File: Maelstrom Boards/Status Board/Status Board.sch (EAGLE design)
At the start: 14 parts, among them P1 39-30-04

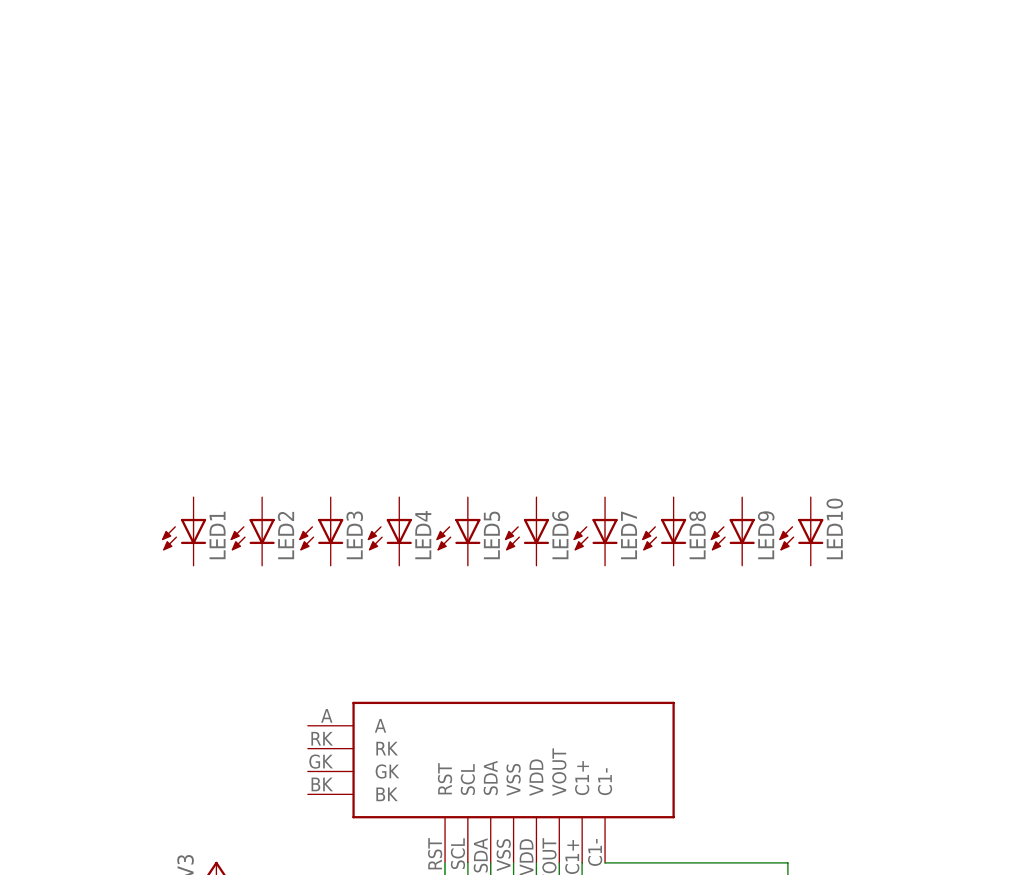
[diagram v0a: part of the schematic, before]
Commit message: Adding LEDs
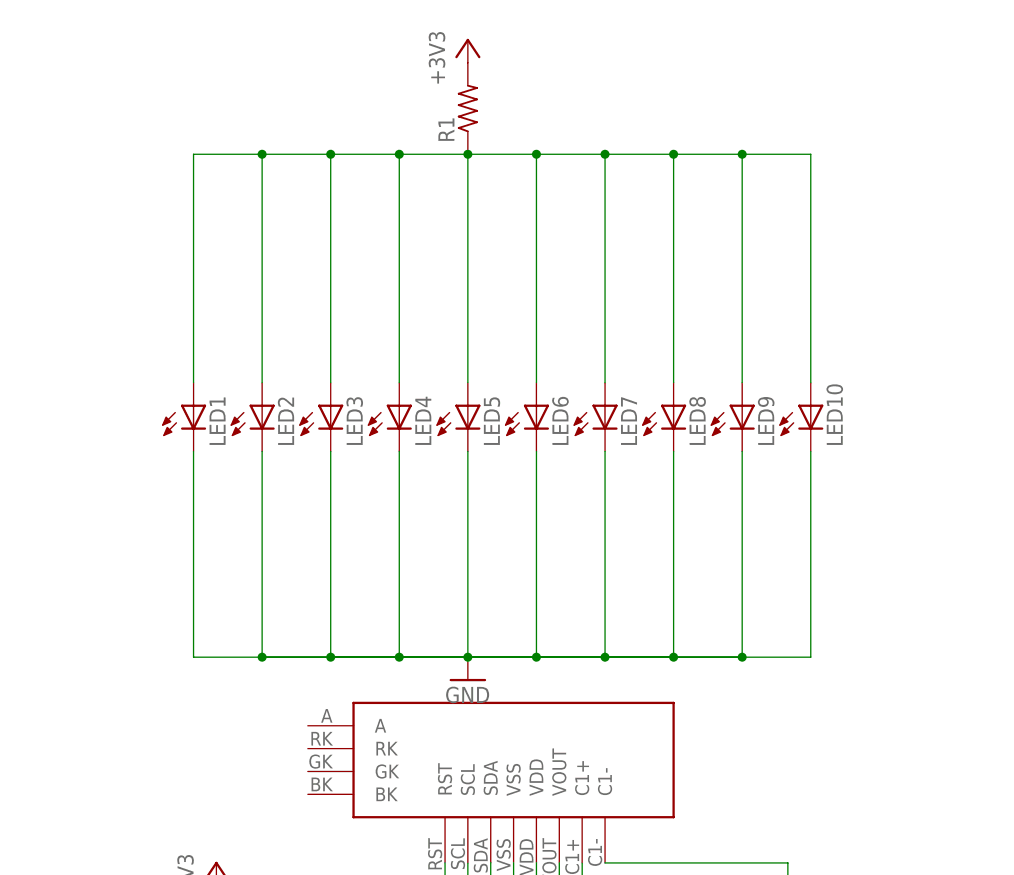
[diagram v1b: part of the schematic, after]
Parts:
- added R1: (no value), rcl:R-US_M3216
- LED1, LED10, LED2, LED3, LED4, LED5, LED6, LED7, LED8, LED9: device led:LEDCHIPLED-0603-TTW -> led:LEDCHIPLED_0603
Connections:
- new net N$4: LED1.A, LED10.A, LED2.A, LED3.A, LED4.A, LED5.A, LED6.A, LED7.A, LED8.A, LED9.A, R1.1
- net +3V3: now also R1.2
- net GND: now also LED1.C, LED10.C, LED2.C, LED3.C, LED4.C, LED5.C, LED6.C, LED7.C, LED8.C, LED9.C
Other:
- moved on the sheet: LED1, LED10, LED2, LED3, LED4, LED5, LED6, LED7, LED8, LED9

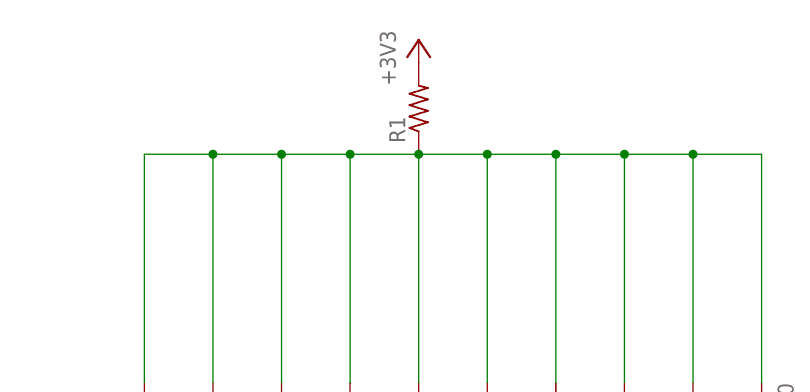
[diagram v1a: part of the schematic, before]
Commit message: Removing Resistor
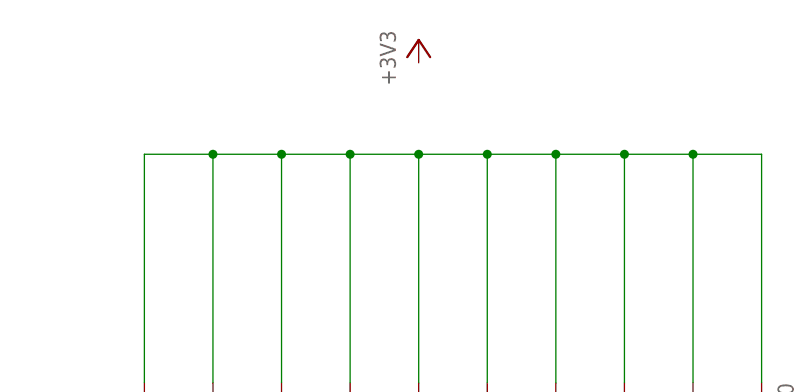
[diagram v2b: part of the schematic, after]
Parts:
- removed R1: (no value), rcl:R-US_M3216
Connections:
- net +3V3: no longer R1.2
- net N$4: no longer R1.1
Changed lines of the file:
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@@
 <part name="LED10" library="led" library_urn="urn:adsk.eagle:library:259" deviceset="LED" device="CHIPLED_0603" package3d_urn="urn:adsk.eagle:package:15822/2"/>
 <part name="GND3" library="supply1" library_urn="urn:adsk.eagle:library:371" deviceset="GND" device=""/>
-<part name="R1" library="rcl" library_urn="urn:adsk.eagle:library:334" deviceset="R-US_" device="M3216" package3d_urn="urn:adsk.eagle:package:23563/1"/>
 <part name="+3V3" library="supply1" library_urn="urn:adsk.eagle:library:371" deviceset="+3V3" device=""/>
 </parts>
@@
 <attribute name="VALUE" x="162.56" y="154.94" size="1.778" layer="96"/>
 </instance>
-<instance part="R1" gate="G$1" x="165.1" y="220.98" smashed="yes" rot="R90">
-<attribute name="NAME" x="163.6014" y="217.17" size="1.778" layer="95" rot="R90"/>
-<attribute name="VALUE" x="168.402" y="217.17" size="1.778" layer="96" rot="R90"/>
-</instance>
 <instance part="+3V3" gate="G$1" x="165.1" y="228.6" smashed="yes">
 <attribute name="VALUE" x="162.56" y="223.52" size="1.778" layer="96" rot="R90"/>
@@
 <wire x1="162.56" y1="137.16" x2="162.56" y2="134.62" width="0.1524" layer="91"/>
 <junction x="162.56" y="134.62"/>
-</segment>
-<segment>
-<pinref part="+3V3" gate="G$1" pin="+3V3"/>
-<pinref part="R1" gate="G$1" pin="2"/>
 </segment>
 </net>
@@
 <junction x="187.96" y="215.9"/>
 <junction x="195.58" y="215.9"/>
-<pinref part="R1" gate="G$1" pin="1"/>
 </segment>
 </net>

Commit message: Update Status Board
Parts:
- added R1: 23.333333, rcl:R-US_M3216
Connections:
- net +3V3: now also R1.2
- net N$4: now also R1.1
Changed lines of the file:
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@@
 <part name="LED10" library="led" library_urn="urn:adsk.eagle:library:259" deviceset="LED" device="CHIPLED_0603" package3d_urn="urn:adsk.eagle:package:15822/2"/>
 <part name="GND3" library="supply1" library_urn="urn:adsk.eagle:library:371" deviceset="GND" device=""/>
+<part name="R1" library="rcl" library_urn="urn:adsk.eagle:library:334" deviceset="R-US_" device="M3216" package3d_urn="urn:adsk.eagle:package:23563/1" value="23.333333"/>
 <part name="+3V3" library="supply1" library_urn="urn:adsk.eagle:library:371" deviceset="+3V3" device=""/>
 </parts>
@@
 <attribute name="VALUE" x="208.915" y="183.388" size="1.778" layer="96" rot="R90"/>
 </instance>
-<instance part="GND3" gate="1" x="165.1" y="157.48" smashed="yes">
-<attribute name="VALUE" x="162.56" y="154.94" size="1.778" layer="96"/>
+<instance part="GND3" gate="1" x="165.1" y="165.1" smashed="yes">
+<attribute name="VALUE" x="162.56" y="162.56" size="1.778" layer="96"/>
+</instance>
+<instance part="R1" gate="G$1" x="165.1" y="220.98" smashed="yes" rot="R90">
+<attribute name="NAME" x="163.6014" y="217.17" size="1.778" layer="95" rot="R90"/>
+<attribute name="VALUE" x="168.402" y="217.17" size="1.778" layer="96" rot="R90"/>
 </instance>
 <instance part="+3V3" gate="G$1" x="165.1" y="228.6" smashed="yes">
@@
 <junction x="162.56" y="134.62"/>
 </segment>
+<segment>
+<pinref part="+3V3" gate="G$1" pin="+3V3"/>
+<pinref part="R1" gate="G$1" pin="2"/>
+</segment>
 </net>
 <net name="GND" class="0">
@@
 <pinref part="LED5" gate="G$1" pin="C"/>
 <pinref part="GND3" gate="1" pin="GND"/>
-<wire x1="165.1" y1="182.88" x2="165.1" y2="160.02" width="0.1524" layer="91"/>
+<wire x1="165.1" y1="182.88" x2="165.1" y2="167.64" width="0.1524" layer="91"/>
 <pinref part="LED4" gate="G$1" pin="C"/>
-<wire x1="157.48" y1="182.88" x2="157.48" y2="160.02" width="0.1524" layer="91"/>
-<wire x1="157.48" y1="160.02" x2="165.1" y2="160.02" width="0.1524" layer="91"/>
-<junction x="165.1" y="160.02"/>
+<wire x1="157.48" y1="182.88" x2="157.48" y2="167.64" width="0.1524" layer="91"/>
+<junction x="165.1" y="167.64"/>
 <pinref part="LED3" gate="G$1" pin="C"/>
-<wire x1="149.86" y1="182.88" x2="149.86" y2="160.02" width="0.1524" layer="91"/>
-<wire x1="149.86" y1="160.02" x2="157.48" y2="160.02" width="0.1524" layer="91"/>
+<wire x1="149.86" y1="182.88" x2="149.86" y2="167.64" width="0.1524" layer="91"/>
 <pinref part="LED2" gate="G$1" pin="C"/>
-<wire x1="157.48" y1="160.02" x2="165.1" y2="160.02" width="0.1524" layer="91"/>
-<wire x1="142.24" y1="182.88" x2="142.24" y2="160.02" width="0.1524" layer="91"/>
-<wire x1="142.24" y1="160.02" x2="149.86" y2="160.02" width="0.1524" layer="91"/>
+<wire x1="142.24" y1="182.88" x2="142.24" y2="167.64" width="0.1524" layer="91"/>
 <pinref part="LED1" gate="G$1" pin="C"/>
-<wire x1="149.86" y1="160.02" x2="157.48" y2="160.02" width="0.1524" layer="91"/>
-<wire x1="157.48" y1="160.02" x2="165.1" y2="160.02" width="0.1524" layer="91"/>
-<wire x1="134.62" y1="182.88" x2="134.62" y2="160.02" width="0.1524" layer="91"/>
-<wire x1="134.62" y1="160.02" x2="142.24" y2="160.02" width="0.1524" layer="91"/>
+<wire x1="134.62" y1="182.88" x2="134.62" y2="167.64" width="0.1524" layer="91"/>
+<wire x1="134.62" y1="167.64" x2="142.24" y2="167.64" width="0.1524" layer="91"/>
 <pinref part="LED6" gate="G$1" pin="C"/>
-<wire x1="142.24" y1="160.02" x2="149.86" y2="160.02" width="0.1524" layer="91"/>
-<wire x1="149.86" y1="160.02" x2="157.48" y2="160.02" width="0.1524" layer="91"/>
-<wire x1="157.48" y1="160.02" x2="165.1" y2="160.02" width="0.1524" layer="91"/>
-<wire x1="172.72" y1="182.88" x2="172.72" y2="160.02" width="0.1524" layer="91"/>
-<wire x1="172.72" y1="160.02" x2="165.1" y2="160.02" width="0.1524" layer="91"/>
+<wire x1="142.24" y1="167.64" x2="149.86" y2="167.64" width="0.1524" layer="91"/>
+<wire x1="149.86" y1="167.64" x2="157.48" y2="167.64" width="0.1524" layer="91"/>
+<wire x1="157.48" y1="167.64" x2="165.1" y2="167.64" width="0.1524" layer="91"/>
+<wire x1="172.72" y1="182.88" x2="172.72" y2="167.64" width="0.1524" layer="91"/>
 <pinref part="LED7" gate="G$1" pin="C"/>
-<wire x1="180.34" y1="182.88" x2="180.34" y2="160.02" width="0.1524" layer="91"/>
-<wire x1="180.34" y1="160.02" x2="172.72" y2="160.02" width="0.1524" layer="91"/>
+<wire x1="180.34" y1="182.88" x2="180.34" y2="167.64" width="0.1524" layer="91"/>
 <pinref part="LED8" gate="G$1" pin="C"/>
-<wire x1="172.72" y1="160.02" x2="165.1" y2="160.02" width="0.1524" layer="91"/>
-<wire x1="187.96" y1="182.88" x2="187.96" y2="160.02" width="0.1524" layer="91"/>
-<wire x1="187.96" y1="160.02" x2="180.34" y2="160.02" width="0.1524" layer="91"/>
+<wire x1="187.96" y1="182.88" x2="187.96" y2="167.64" width="0.1524" layer="91"/>
 <pinref part="LED9" gate="G$1" pin="C"/>
-<wire x1="180.34" y1="160.02" x2="172.72" y2="160.02" width="0.1524" layer="91"/>
-<wire x1="172.72" y1="160.02" x2="165.1" y2="160.02" width="0.1524" layer="91"/>
-<wire x1="195.58" y1="182.88" x2="195.58" y2="160.02" width="0.1524" layer="91"/>
-<wire x1="195.58" y1="160.02" x2="187.96" y2="160.02" width="0.1524" layer="91"/>
+<wire x1="195.58" y1="182.88" x2="195.58" y2="167.64" width="0.1524" layer="91"/>
 <pinref part="LED10" gate="G$1" pin="C"/>
-<wire x1="187.96" y1="160.02" x2="180.34" y2="160.02" width="0.1524" layer="91"/>
-<wire x1="180.34" y1="160.02" x2="172.72" y2="160.02" width="0.1524" layer="91"/>
-<wire x1="172.72" y1="160.02" x2="165.1" y2="160.02" width="0.1524" layer="91"/>
-<wire x1="203.2" y1="182.88" x2="203.2" y2="160.02" width="0.1524" layer="91"/>
-<wire x1="203.2" y1="160.02" x2="195.58" y2="160.02" width="0.1524" layer="91"/>
-<junction x="195.58" y="160.02"/>
-<wire x1="195.58" y1="160.02" x2="187.96" y2="160.02" width="0.1524" layer="91"/>
-<junction x="187.96" y="160.02"/>
-<wire x1="187.96" y1="160.02" x2="180.34" y2="160.02" width="0.1524" layer="91"/>
-<junction x="180.34" y="160.02"/>
-<wire x1="180.34" y1="160.02" x2="172.72" y2="160.02" width="0.1524" layer="91"/>
-<junction x="172.72" y="160.02"/>
-<wire x1="172.72" y1="160.02" x2="165.1" y2="160.02" width="0.1524" layer="91"/>
-<junction x="157.48" y="160.02"/>
-<junction x="149.86" y="160.02"/>
-<junction x="142.24" y="160.02"/>
+<wire x1="203.2" y1="182.88" x2="203.2" y2="167.64" width="0.1524" layer="91"/>
+<wire x1="203.2" y1="167.64" x2="195.58" y2="167.64" width="0.1524" layer="91"/>
+<junction x="195.58" y="167.64"/>
+<wire x1="195.58" y1="167.64" x2="187.96" y2="167.64" width="0.1524" layer="91"/>
+<junction x="187.96" y="167.64"/>
+<wire x1="187.96" y1="167.64" x2="180.34" y2="167.64" width="0.1524" layer="91"/>
+<junction x="180.34" y="167.64"/>
+<wire x1="180.34" y1="167.64" x2="172.72" y2="167.64" width="0.1524" layer="91"/>
+<junction x="172.72" y="167.64"/>
+<wire x1="172.72" y1="167.64" x2="165.1" y2="167.64" width="0.1524" layer="91"/>
+<junction x="157.48" y="167.64"/>
+<junction x="149.86" y="167.64"/>
+<junction x="142.24" y="167.64"/>
 </segment>
 </net>
@@
 <junction x="187.96" y="215.9"/>
 <junction x="195.58" y="215.9"/>
+<pinref part="R1" gate="G$1" pin="1"/>
 </segment>
 </net>

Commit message: Finished status board schematic
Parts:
- added C3: 1uF, rcl:C-EUC0603
- added C4: 0.1uF, rcl:C-EUC0603
- added IC1: LM555D, linear:LM555D
- added Q1: 310mA/60V/1.6Ω, SparkFun-DiscreteSemi:MOSFET-NCH-2N7002PW
- added R2: 70, rcl:R-US_R0603
- added R3, R4: 15, rcl:R-US_R0603
- added R5: 50k, rcl:R-US_R0603
- added R6: 100k, rcl:R-US_R0603
- added R7: 10k, rcl:R-US_R0603
- added RG, RV+: 0, rcl:R-US_R0603
- added U$2: MAX7315, MAX7315:MAX7315
- C1, C2: value (none) -> 1uF
- R1: value 23.333333 -> 6.8; device rcl:R-US_M3216 -> rcl:R-US_R0603
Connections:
- new net BLINK: IC1.Q, Q1.G
- new net BLINK_OFF: IC1.R, R7.2, U$2.P3
- new net BLUE: R4.2, U$2.P2
- new net GREEN: R3.2, U$2.P1
- new net N$10: C3.1, IC1.THR, IC1.TR, R5.2, R6.1
- new net N$20: LED1.C, LED10.C, LED2.C, LED3.C, LED4.C, LED5.C, LED6.C, LED7.C, LED8.C, LED9.C, Q1.D
- new net N$4: C2.2, U$1.C1+
- new net N$5: R3.1, U$1.GK
- new net N$6: RG.2, RV+.1, U$2.AD0, U$2.AD1, U$2.AD2
- new net N$7: R2.1, U$1.RK
- new net N$9: IC1.DIS, R5.1
- new net RED: R2.2, U$2.P0
- net +3V3: now also C4.1, IC1.V+, R6.2, R7.1, RV+.2, U$1.A, U$2.V+
- net GND: now also C3.2, C4.2, IC1.GND, Q1.S, RG.1, U$2.GND; no longer LED1.C, LED10.C, LED2.C, LED3.C, LED4.C, LED5.C, LED6.C, LED7.C, LED8.C, LED9.C
- net N$1: now also R4.1, U$1.BK; no longer C2.1, U$1.C1+
- net N$2: now also C2.1; no longer C2.2
- net SCL: now also U$2.SCL
- net SDA: now also U$2.SDA
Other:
- note added: "Blinking Circuit"
- note added: "Input Connector"
- note added: "Light Controller"
- note added: "Screen"
- note added: "Warning LEDs"
- moved on the sheet: C1, C2, LED1, LED10, LED2, LED3, LED4, LED5, LED6, LED7, LED8, LED9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
